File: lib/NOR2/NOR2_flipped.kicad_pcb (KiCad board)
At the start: 2 copper layers, 4 parts

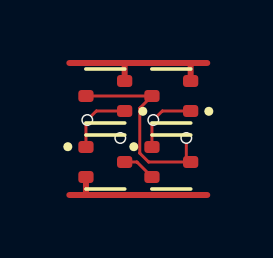
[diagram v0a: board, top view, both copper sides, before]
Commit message: All cells now use 1mm*4mm grid rather than 1.1mm*4.4mm
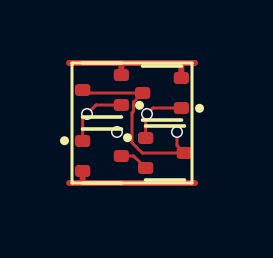
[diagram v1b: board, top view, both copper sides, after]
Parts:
- moved P2 0.37 mm to (3.10, 3.00)
- moved N2 0.33 mm to (3.00, 1.00)
- moved N1 0.23 mm to (1.00, 0.90)
- moved P1 0.23 mm to (1.00, 3.10)
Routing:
- net GND: track 5.81 -> 5.15 mm
- net VDD: track 5.21 -> 4.62 mm
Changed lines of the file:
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@@
 	(footprint "Package_TO_SOT_SMD:SOT-523"
 		(layer "F.Cu")
-		(at 3.31 1.1 180)
+		(at 3 1 180)
 		(descr "SOT523, https://www.diodes.com/assets/Package-Files/SOT523.pdf")
 		(tags "SOT-523")
@@
 	(footprint "Package_TO_SOT_SMD:SOT-523"
 		(layer "F.Cu")
-		(at 1.11 1.1 180)
+		(at 1 0.9 180)
 		(descr "SOT523, https://www.diodes.com/assets/Package-Files/SOT523.pdf")
 		(tags "SOT-523")
@@
 	(footprint "Package_TO_SOT_SMD:SOT-523"
 		(layer "F.Cu")
-		(at 3.31 3.3)
+		(at 3.1 3)
 		(descr "SOT523, https://www.diodes.com/assets/Package-Files/SOT523.pdf")
 		(tags "SOT-523")
@@
 	(footprint "Package_TO_SOT_SMD:SOT-523"
 		(layer "F.Cu")
-		(at 1.11 3.3)
+		(at 1 3.1)
 		(descr "SOT523, https://www.diodes.com/assets/Package-Files/SOT523.pdf")
 		(tags "SOT-523")
@@
 		)
 	)
+	(gr_rect
+		(start 0 0)
+		(end 4 4)
+		(stroke
+			(width 0.1)
+			(type default)
+		)
+		(fill no)
+		(layer "F.SilkS")
+	)
 	(via
-		(at 1.61 2.5)
+		(at 1.5 2.3)
 		(size 0.4)
 		(drill 0.3)
@@
 	)
 	(segment
+		(start 3.645 0.5)
+		(end 3.645 0.055)
+		(width 0.2)
+		(layer "F.Cu")
+		(net 1)
+	)
+	(segment
+		(start 1.6 0)
+		(end 1.76 0)
+		(width 0.2)
+		(layer "F.Cu")
+		(net 1)
+	)
+	(segment
+		(start 1.645 0.045)
+		(end 1.6 0)
+		(width 0.2)
+		(layer "F.Cu")
+		(net 1)
+	)
+	(segment
+		(start 3.645 0.055)
+		(end 3.7 0)
+		(width 0.2)
+		(layer "F.Cu")
+		(net 1)
+	)
+	(segment
 		(start 1.76 0)
-		(end 3.97 0)
+		(end 3.7 0)
 		(width 0.2)
 		(layer "F.Cu")
@@
 	)
 	(segment
-		(start 1.755 0.6)
-		(end 1.755 0.005)
+		(start 3.7 0)
+		(end 4.1 0)
 		(width 0.2)
 		(layer "F.Cu")
@@
 	)
 	(segment
-		(start 3.97 0)
-		(end 4.51 0)
+		(start -0.1 0)
+		(end 1.6 0)
 		(width 0.2)
 		(layer "F.Cu")
@@
 	)
 	(segment
-		(start 3.955 0.6)
-		(end 3.955 0.015)
+		(start 1.645 0.4)
+		(end 1.645 0.045)
 		(width 0.2)
 		(layer "F.Cu")
@@
 	)
 	(segment
-		(start 3.955 0.015)
-		(end 3.97 0)
-		(width 0.2)
-		(layer "F.Cu")
-		(net 1)
-	)
-	(segment
-		(start -0.09 0)
-		(end 1.76 0)
-		(width 0.2)
-		(layer "F.Cu")
-		(net 1)
-	)
-	(segment
-		(start 2.259 1.506)
-		(end 2.665 1.1)
+		(start 2 2.657738)
+		(end 2 1.657738)
 		(width 0.1)
 		(layer "F.Cu")
@@
 	)
 	(segment
-		(start 2.552262 3.3)
-		(end 2.259 3.006738)
+		(start 3.5 2.3)
+		(end 3.5 2.755)
 		(width 0.1)
 		(layer "F.Cu")
@@
 	)
 	(segment
-		(start 2.665 1.1)
-		(end 0.465 1.1)
+		(start 2.051 1.304)
+		(end 2.355 1)
 		(width 0.1)
 		(layer "F.Cu")
@@
 	)
 	(segment
-		(start 3.955 3.3)
-		(end 2.552262 3.3)
+		(start 2 1.657738)
+		(end 2.051 1.606738)
 		(width 0.1)
 		(layer "F.Cu")
@@
 	)
 	(segment
-		(start 3.81 2.5)
-		(end 3.81 3.155)
+		(start 3.5 2.755)
+		(end 3.745 3)
 		(width 0.1)
 		(layer "F.Cu")
@@
 	)
 	(segment
-		(start 3.81 3.155)
-		(end 3.955 3.3)
+		(start 0.355 1)
+		(end 2.355 1)
 		(width 0.1)
 		(layer "F.Cu")
@@
 	)
 	(segment
-		(start 2.259 3.006738)
-		(end 2.259 1.506)
+		(start 3.745 3)
+		(end 2.342262 3)
 		(width 0.1)
 		(layer "F.Cu")
 		(net 2)
 	)
+	(segment
+		(start 2.051 1.606738)
+		(end 2.051 1.304)
+		(width 0.1)
+		(layer "F.Cu")
+		(net 2)
+	)
+	(segment
+		(start 2.342262 3)
+		(end 2 2.657738)
+		(width 0.1)
+		(layer "F.Cu")
+		(net 2)
+	)
 	(via
-		(at 3.81 2.5)
+		(at 3.5 2.3)
 		(size 0.4)
 		(drill 0.3)
@@
 	)
 	(segment
-		(start 2.165 3.3)
-		(end 2.665 3.8)
+		(start 2.055 3.1)
+		(end 2.455 3.5)
 		(width 0.1)
 		(layer "F.Cu")
@@
 	)
 	(segment
-		(start 1.755 3.3)
-		(end 2.165 3.3)
+		(start 1.645 3.1)
+		(end 2.055 3.1)
 		(width 0.1)
 		(layer "F.Cu")
@@
 	)
 	(segment
-		(start 0.47 4.4)
-		(end 2.66 4.4)
+		(start 0.47 4)
+		(end 2.66 4)
 		(width 0.2)
 		(layer "F.Cu")
@@
 	)
 	(segment
-		(start 0.465 3.8)
-		(end 0.465 4.395)
+		(start 0.355 3.6)
+		(end 0.355 3.955)
 		(width 0.2)
 		(layer "F.Cu")
@@
 	)
 	(segment
-		(start 2.66 4.4)
-		(end 4.51 4.4)
+		(start 2.66 4)
+		(end 4.1 4)
 		(width 0.2)
 		(layer "F.Cu")
@@
 	)
 	(segment
-		(start -0.09 4.4)
-		(end 0.47 4.4)
+		(start 0.4 4)
+		(end 0.47 4)
 		(width 0.2)
 		(layer "F.Cu")
@@
 	)
 	(segment
-		(start 0.465 4.395)
-		(end 0.47 4.4)
+		(start -0.1 4)
+		(end 0.4 4)
 		(width 0.2)
 		(layer "F.Cu")
@@
 	)
 	(segment
-		(start 2.665 4.395)
-		(end 2.66 4.4)
+		(start 0.355 3.955)
+		(end 0.4 4)
 		(width 0.2)
 		(layer "F.Cu")
@@
 	)
 	(segment
-		(start 0.465 1.945)
-		(end 0.51 1.9)
+		(start 2.665 4)
+		(end 2.66 4)
+		(width 0.2)
+		(layer "F.Cu")
+		(net 4)
+	)
+	(segment
+		(start 0.355 1.845)
+		(end 0.5 1.7)
 		(width 0.1)
 		(layer "F.Cu")
@@
 	)
 	(segment
-		(start 0.81 1.6)
-		(end 0.51 1.9)
+		(start 0.355 2.6)
+		(end 0.355 1.845)
 		(width 0.1)
 		(layer "F.Cu")
@@
 	)
 	(segment
-		(start 0.465 2.8)
-		(end 0.465 1.945)
+		(start 1.645 1.4)
+		(end 0.8 1.4)
 		(width 0.1)
 		(layer "F.Cu")
@@
 	)
 	(segment
-		(start 1.755 1.6)
-		(end 0.81 1.6)
+		(start 0.8 1.4)
+		(end 0.5 1.7)
 		(width 0.1)
 		(layer "F.Cu")
@@
 	)
 	(via
-		(at 0.51 1.9)
+		(at 0.5 1.7)
 		(size 0.4)
 		(drill 0.3)
@@
 	)
 	(segment
-		(start 3.955 1.6)
-		(end 3.01 1.6)
+		(start 2.7 1.5)
+		(end 2.5 1.7)
 		(width 0.1)
 		(layer "F.Cu")
@@
 	)
 	(segment
-		(start 2.665 1.945)
-		(end 2.71 1.9)
+		(start 2.455 1.745)
+		(end 2.5 1.7)
 		(width 0.1)
 		(layer "F.Cu")
@@
 	)
 	(segment
-		(start 2.665 2.8)
-		(end 2.665 1.945)
+		(start 3.645 1.5)
+		(end 2.7 1.5)
 		(width 0.1)
 		(layer "F.Cu")
@@
 	)
 	(segment
-		(start 3.01 1.6)
-		(end 2.71 1.9)
+		(start 2.455 2.5)
+		(end 2.455 1.745)
 		(width 0.1)
 		(layer "F.Cu")
@@
 	)
 	(via
-		(at 2.71 1.9)
+		(at 2.5 1.7)
 		(size 0.4)
 		(drill 0.3)

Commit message: Make the pads of my SOT523 footprint very slightly smaller, which is enough to route all the cells and leave the mosfets exactly on the grid
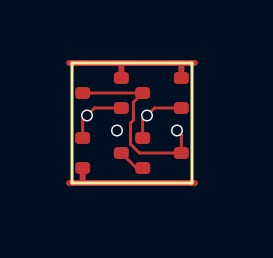
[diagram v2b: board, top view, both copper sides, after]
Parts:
- N1, N2, P1, P2: footprint Package_TO_SOT_SMD:SOT-523 -> RV523:SOT523
- moved P1 0.10 mm to (1.00, 3.00)
- moved P2 0.10 mm to (3.00, 3.00)
- moved N1 0.10 mm to (1.00, 1.00)

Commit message: Propagate MOSFET values to the cells' PCBs
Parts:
- N1, N2: value (none) -> NMOS
- P1, P2: value (none) -> PMOS
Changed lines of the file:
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@@
 			)
 		)
-		(property "Value" ""
+		(property "Value" "NMOS"
 			(at 0 0 180)
 			(layer "F.Fab")
@@
 			)
 		)
-		(property "Value" ""
+		(property "Value" "NMOS"
 			(at 0 0 180)
 			(layer "F.Fab")
@@
 			)
 		)
-		(property "Value" ""
+		(property "Value" "PMOS"
 			(at 0 0 0)
 			(layer "F.Fab")
@@
 			)
 		)
-		(property "Value" ""
+		(property "Value" "PMOS"
 			(at 0 0 0)
 			(layer "F.Fab")
